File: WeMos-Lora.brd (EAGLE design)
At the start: 28.6 x 25.7 mm, 9 parts

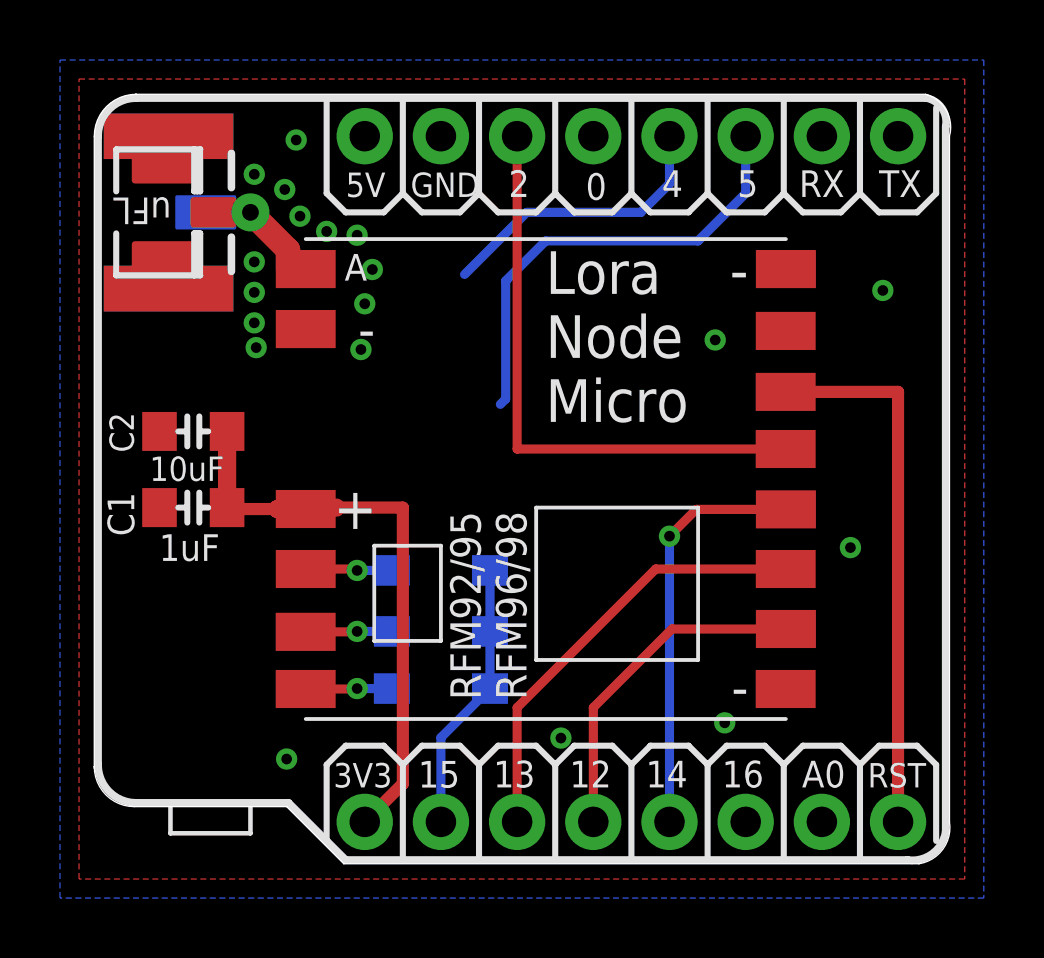
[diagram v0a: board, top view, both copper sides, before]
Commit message: Remove useless routes
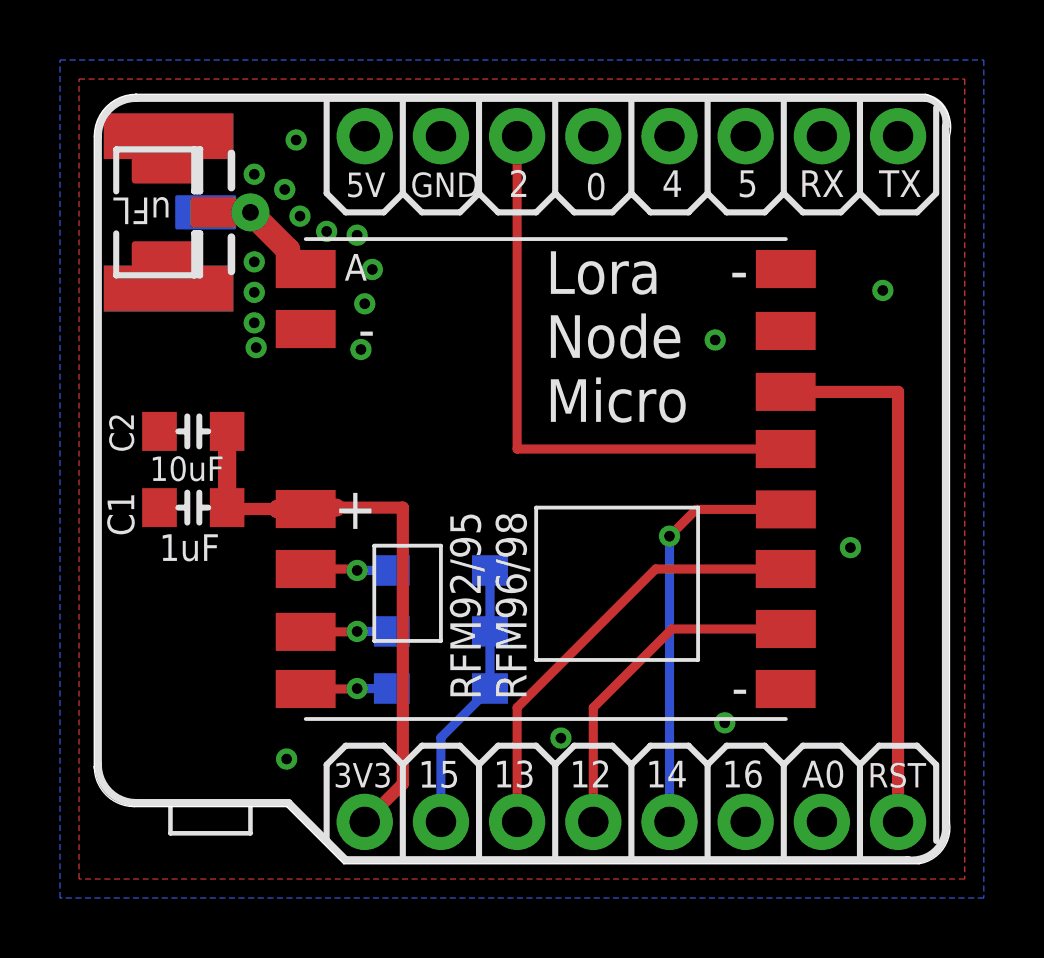
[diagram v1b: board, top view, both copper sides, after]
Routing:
- net SCL: track 15.3 -> 0.00 mm
- net SDA: track 9.67 -> 0.00 mm
